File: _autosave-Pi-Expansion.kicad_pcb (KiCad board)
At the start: 2 copper layers, 56 x 65 mm, 18 parts, among them J1 RPi_GPIO, J2 SMA_H, P1 BATT, Q1 IRLML6344TRPBF, U1 A2200-A, U2 SPX2920U-5.0

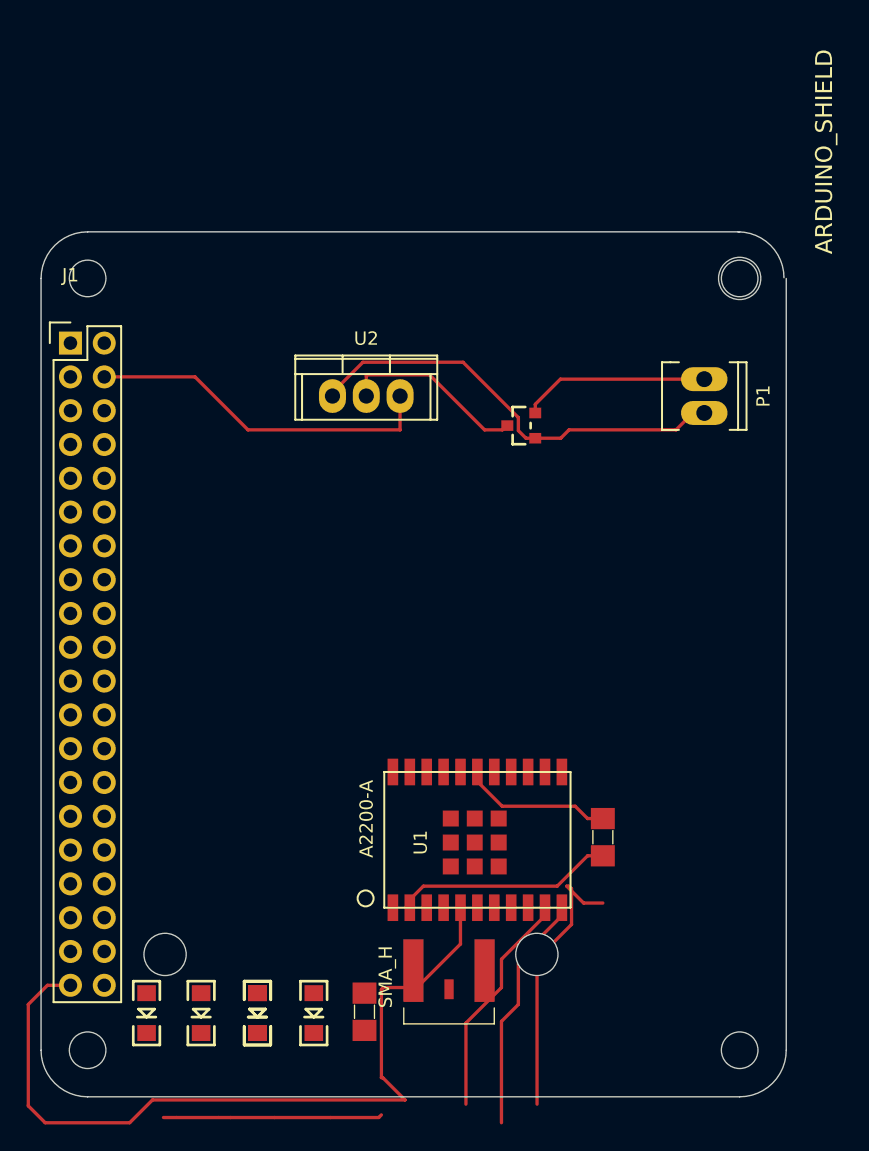
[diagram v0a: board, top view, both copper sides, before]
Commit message: fixed board outline, moved gps
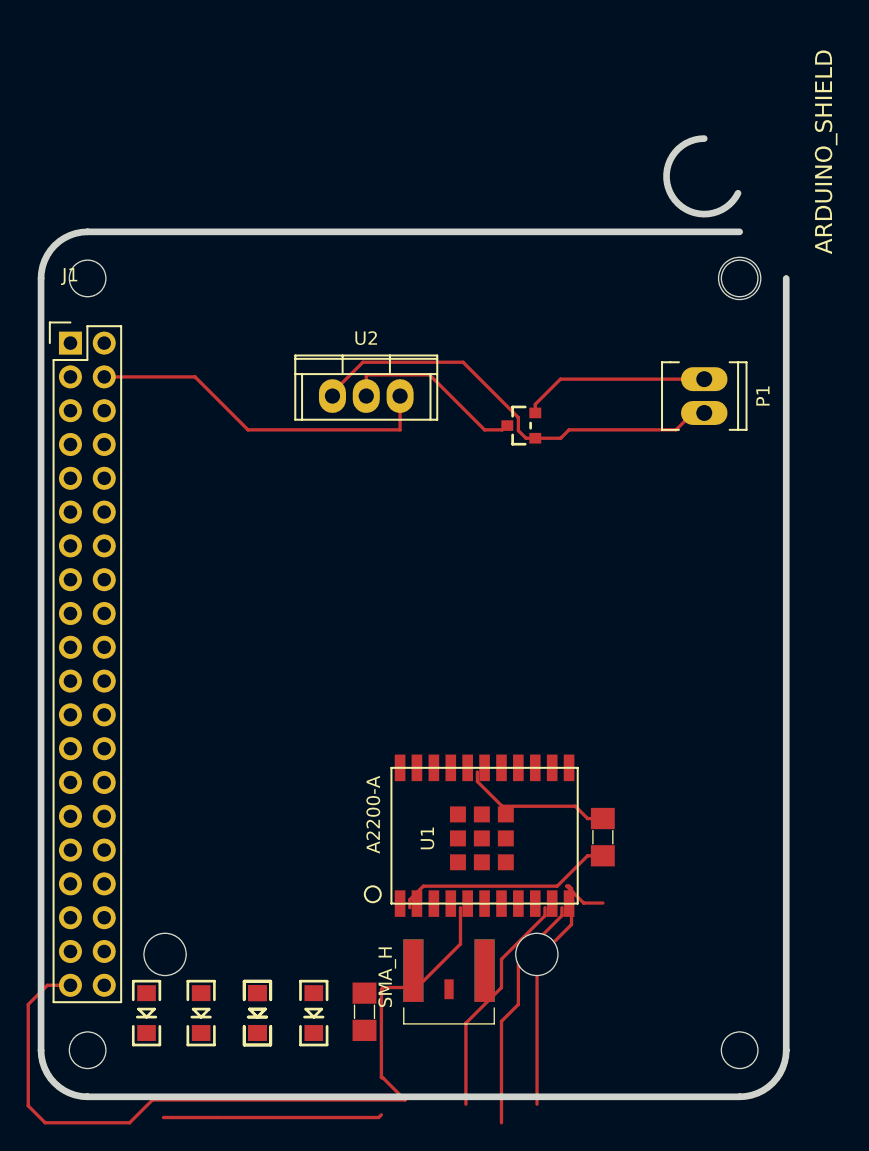
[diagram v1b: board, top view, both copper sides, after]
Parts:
- moved U1 0.62 mm to (70.9, 127.2)
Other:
- board size 56 x 65 mm -> 56 x 72 mm
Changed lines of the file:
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@@
     (links 34)
     (no_connects 25)
-    (area 37.739999 81.589999 93.840001 146.690001)
+    (area 37.539999 81.389999 94.040001 146.890001)
     (thickness 1.6)
-    (drawings 8)
+    (drawings 9)
     (tracks 75)
     (zones 0)
@@
   (page A4)
   (layers
-    (0 F.Cu signal hide)
-    (31 B.Cu signal hide)
+    (0 F.Cu signal)
+    (31 B.Cu signal)
     (32 B.Adhes user hide)
     (33 F.Adhes user hide)
@@
     (36 B.SilkS user hide)
     (37 F.SilkS user hide)
-    (38 B.Mask user hide)
-    (39 F.Mask user hide)
+    (38 B.Mask user)
+    (39 F.Mask user)
     (40 Dwgs.User user hide)
     (41 Cmts.User user hide)
@@
     (trace_min 0.2)
     (segment_width 0.2)
-    (edge_width 0.1)
+    (edge_width 0.5)
     (via_size 0.6)
     (via_drill 0.4)
@@
   )
   (module A2200-A:A2200-A (layer F.Cu)
-    (at 70.38 127.53 90)
+    (at 70.92 127.22 90)
     (tags "GPS Receiver A2200-A")
     (fp_text reference U1 (at 0 -4.064 90) (layer F.SilkS)
@@
     (pad "" np_thru_hole circle (at 15.24 -50.8) (size 3.175 3.175) (drill 3.175) (layers *.Cu *.Mask F.SilkS))
   )
-  (gr_line (start 93.79 143.14) (end 93.79 85.14) (layer Edge.Cuts) (width 0.1))
-  (gr_line (start 41.29 81.64) (end 90.29 81.64) (layer Edge.Cuts) (width 0.1))
-  (gr_line (start 37.79 143.14) (end 37.79 85.14) (layer Edge.Cuts) (width 0.1))
-  (gr_line (start 41.29 146.64) (end 90.29 146.64) (layer Edge.Cuts) (width 0.1))
-  (gr_arc (start 90.29 143.14) (end 93.79 143.14) (angle 90) (layer Edge.Cuts) (width 0.1))
-  (gr_arc (start 41.29 85.14) (end 37.79 85.14) (angle 90) (layer Edge.Cuts) (width 0.1))
-  (gr_arc (start 41.29 143.14) (end 41.29 146.64) (angle 90) (layer Edge.Cuts) (width 0.1))
-  (gr_arc (start 90.17 85.09) (end 90.17 81.64) (angle 90) (layer Edge.Cuts) (width 0.1))
+  (gr_arc (start 87.63 77.47) (end 90.17 78.74) (angle 243.4349488) (layer Edge.Cuts) (width 0.5))
+  (gr_circle (center 93.79 85.14) (end 104.14 111.76) (layer Cmts.User) (width 0.2))
+  (gr_line (start 93.79 143.14) (end 93.79 85.14) (layer Edge.Cuts) (width 0.5))
+  (gr_line (start 41.29 81.64) (end 90.29 81.64) (layer Edge.Cuts) (width 0.5))
+  (gr_line (start 37.79 143.14) (end 37.79 85.14) (layer Edge.Cuts) (width 0.5))
+  (gr_line (start 41.29 146.64) (end 90.29 146.64) (layer Edge.Cuts) (width 0.5))
+  (gr_arc (start 90.29 143.14) (end 93.79 143.14) (angle 90) (layer Edge.Cuts) (width 0.5))
+  (gr_arc (start 41.29 85.14) (end 37.79 85.14) (angle 90) (layer Edge.Cuts) (width 0.5))
+  (gr_arc (start 41.29 143.14) (end 41.29 146.64) (angle 90) (layer Edge.Cuts) (width 0.5))
   (segment (start 75.06208 147.193) (end 75.06208 135.75792) (width 0.25) (layer F.Cu) (net 0))
   (segment (start 77.47 130.81) (end 77.295002 130.81) (width 0.25) (layer F.Cu) (net 0))
@@
   (segment (start 62.30501 92.38499) (end 62.23 92.46) (width 0.25) (layer F.Cu) (net 38))
   (segment (start 62.23 92.46) (end 62.23 93.98) (width 0.25) (layer F.Cu) (net 38))
-  (segment (start 63.5 138.43) (end 63.366219 138.563781) (width 0.25) (layer F.Cu) (net 40))
+  (segment (start 63.5 138.43) (end 63.366219 138.563781) (width 0.25) (layer F.Cu) (net 38))
   (segment (start 66.04 138.43) (end 63.5 138.43) (width 0.25) (layer F.Cu) (net 40))
   (segment (start 69.31 135.16) (end 66.04 138.43) (width 0.25) (layer F.Cu) (net 40))
